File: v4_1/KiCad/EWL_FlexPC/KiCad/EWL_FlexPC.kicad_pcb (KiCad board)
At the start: 2 copper layers, 14.6 x 14.6 mm, 0 parts

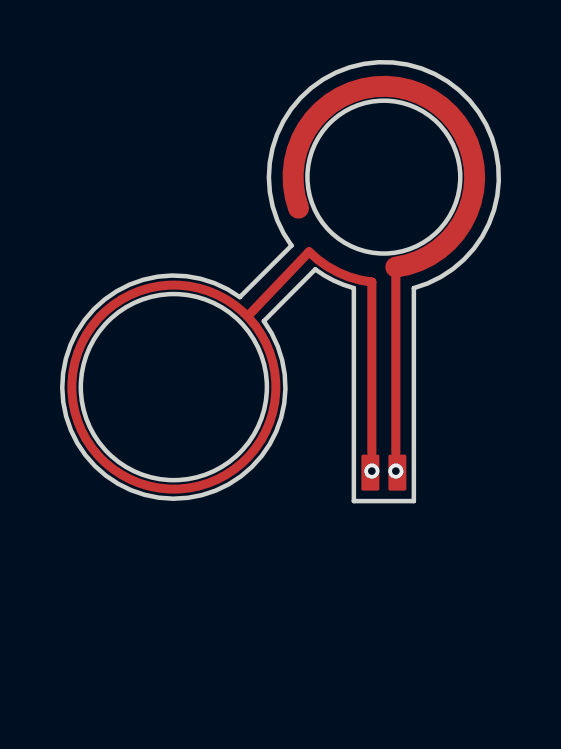
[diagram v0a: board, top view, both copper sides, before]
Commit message: Updates to the project
- Added code to test the functionality of the v4 WF and validate the design
- Fixed a bug that left the EWL run continuously even if it was not recording. Now once the recording ends the EWL goes to sleep mode
- Modified the threshold for which the recording stops once the battery ADC reading reaches certain value
- Fixed a typo on the jupyter notebook name
- Fixed the programming cable by changing the target programming pins footprint
- Added a folder with a KiCAD project for the EWL cable
- For both things I generated new gerbers, which I checked using the gerber viewer
- Not uploaded to the repo due to size constrains: videos demonstrating that the Miniscope can record continuously for over 20 minutes

To do (in the short term):

- Add requirements to create a conda environment for easier use of the DAQ notebook
- Clean a bit more the code
- Add to the documentation the fix we applied to fix the bug that prevented the Miniscope to not run on Release mode
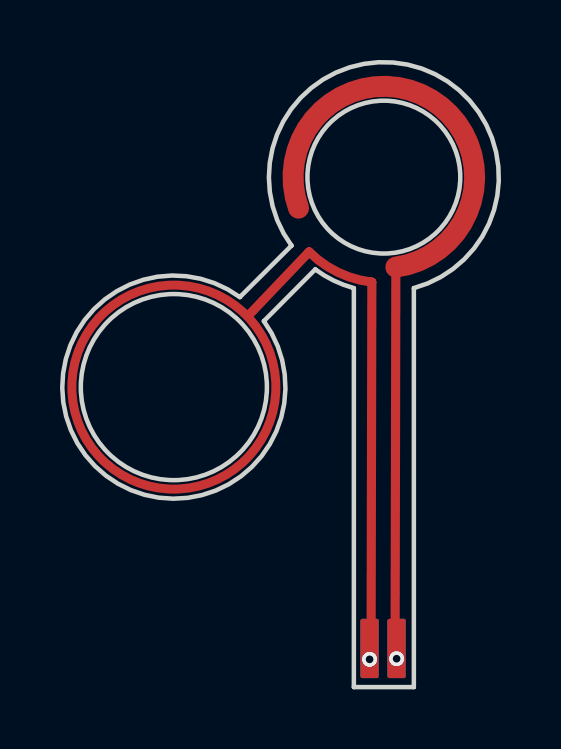
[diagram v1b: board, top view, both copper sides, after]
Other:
- board size 14.6 x 14.6 mm -> 14.6 x 20.8 mm
- net class Default removed
- rule pad_to_mask_clearance: 0.051 -> 0
- board text added: "FH19C Series Thickness : 0.2 ± 0.03mm Gold plated"
